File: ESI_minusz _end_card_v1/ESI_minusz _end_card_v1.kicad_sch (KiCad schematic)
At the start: 32 parts, among them J1 J-SAMTEC-TFM-120-01-L-D-RA, J2 U.FL-R-SMT-1, J3 M55-7101242R, J5 M55-7101242R, U1 BALUN

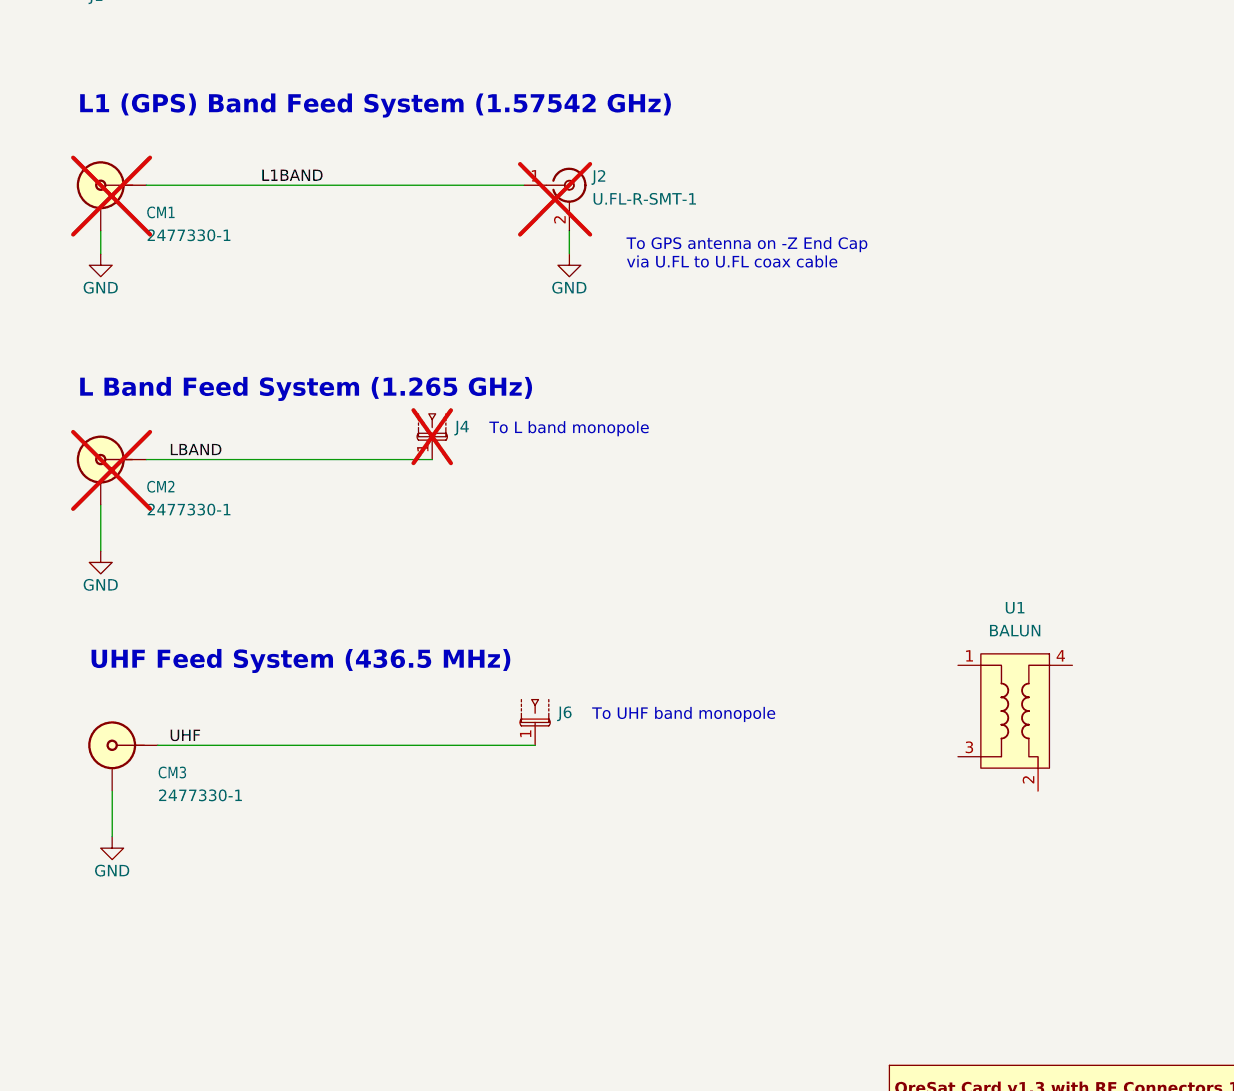
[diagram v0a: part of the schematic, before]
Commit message: Dipole schematic: added balun & footprints. Pre-tracing
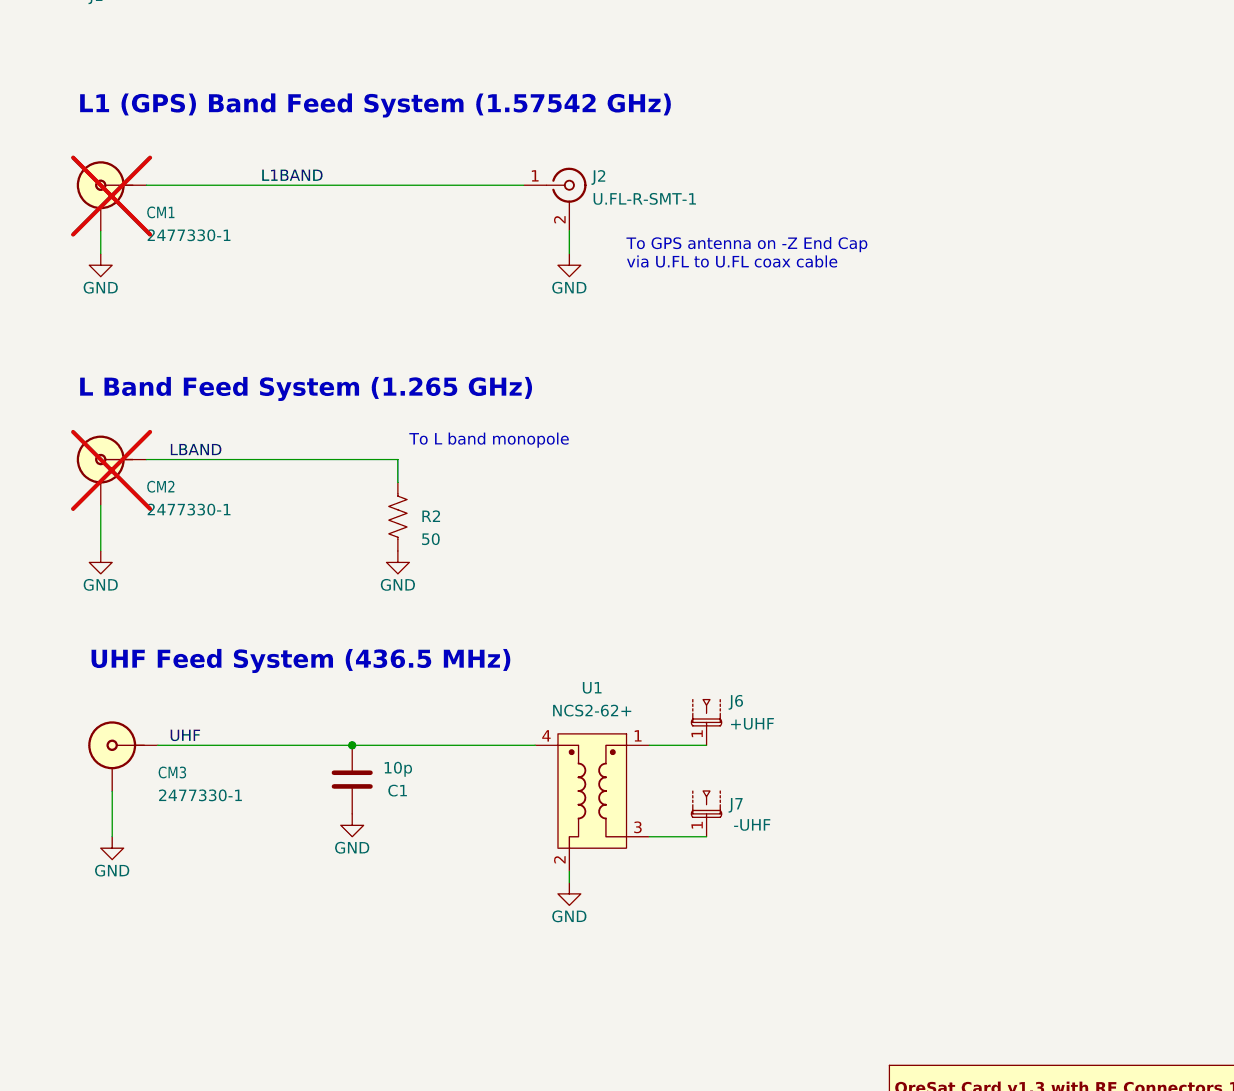
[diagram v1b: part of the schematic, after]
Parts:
- removed J4: ~, oresat-misc:tape-measure-slot-antenna, symbol oresat-misc:tape-measure-antenna
- added C1: 10p, oresat-passives:0402-C-NOSILK, symbol Device:C
- added J7: -UHF, oresat-misc:tape-measure-slot-antenna, symbol oresat-misc:tape-measure-antenna
- added R2: 50, oresat-passives:0805-C-NOSILK, symbol Device:R_US
- J2: now fitted
- J6: value ~ -> +UHF
- U1: value BALUN -> NCS2-62+; footprint (none) -> oresat-passives:2450FB15A050E_JOT; DIS (none) -> Digikey; DPN (none) -> 3157-NCS2-62+TR-ND; MFR (none) -> Mini-Circuits; MPN (none) -> NCS2-62+
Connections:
- net GND: now also C1.1, R2.2
- net LBAND: now also R2.1
- net UHF: now also U1.4, C1.2; no longer J6.1
- net at U1.1: now also J6.1
- net at U1.3: now also J7.1
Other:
- note removed: "To UHF band monopole"
